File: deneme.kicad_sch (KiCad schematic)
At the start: 60 parts, among them J1 USB_C_Receptacle_USB2.0_16P, J2 Conn_01x04_Pin, J3 LORA_USART2_SOCKETS, J4 RJ45, SW1 SW_SPDT, U1 STM32F103C8T6, U2 AMS1117-3.3, U3 MAX485E, U4 ESDS302DBVR, U5 USBLC6-2SC6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

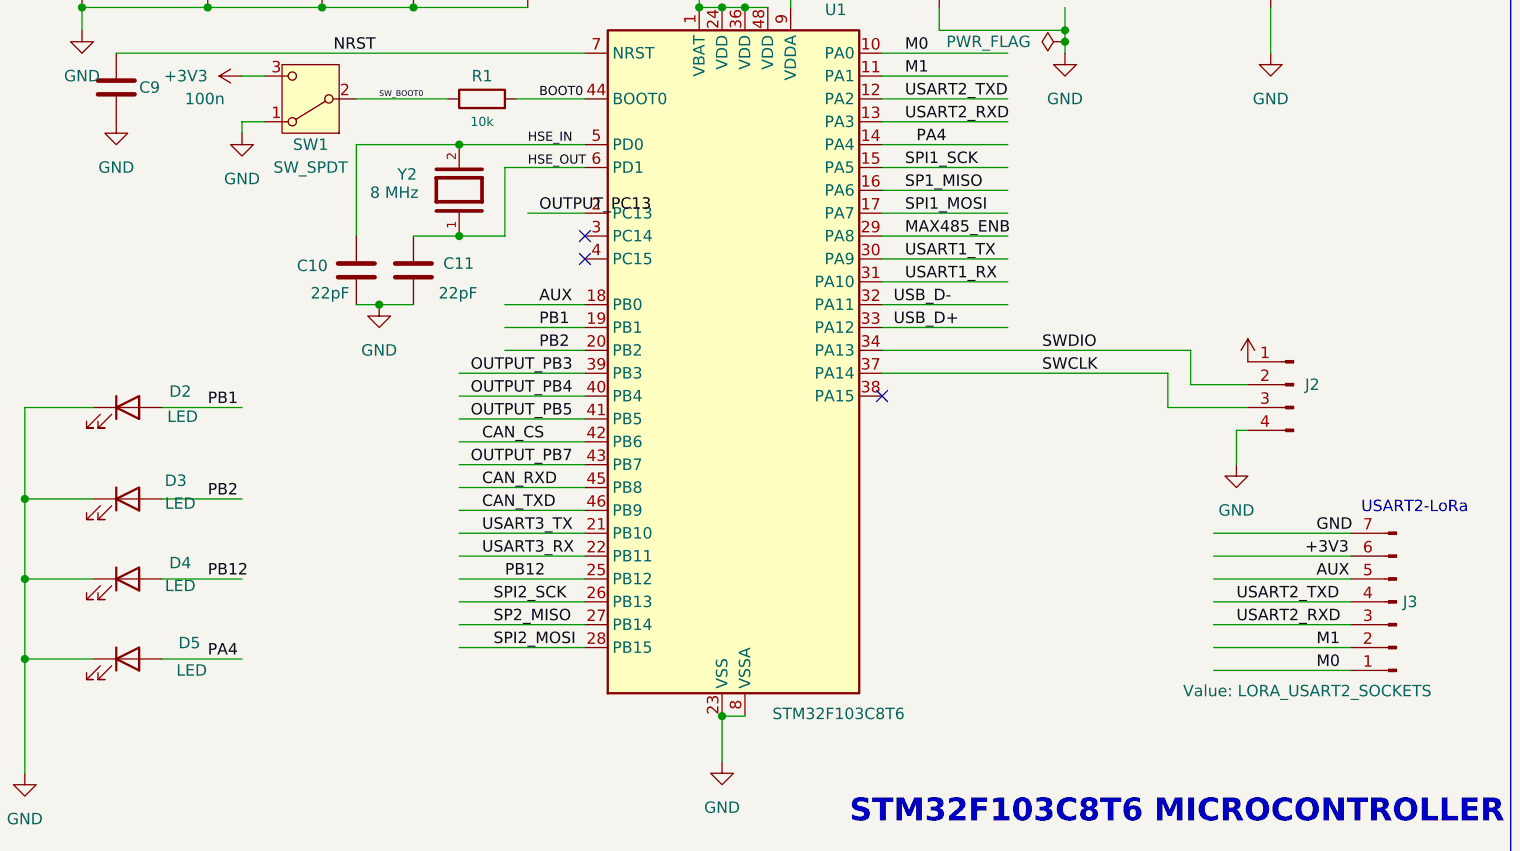
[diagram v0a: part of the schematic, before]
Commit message: added led resistors
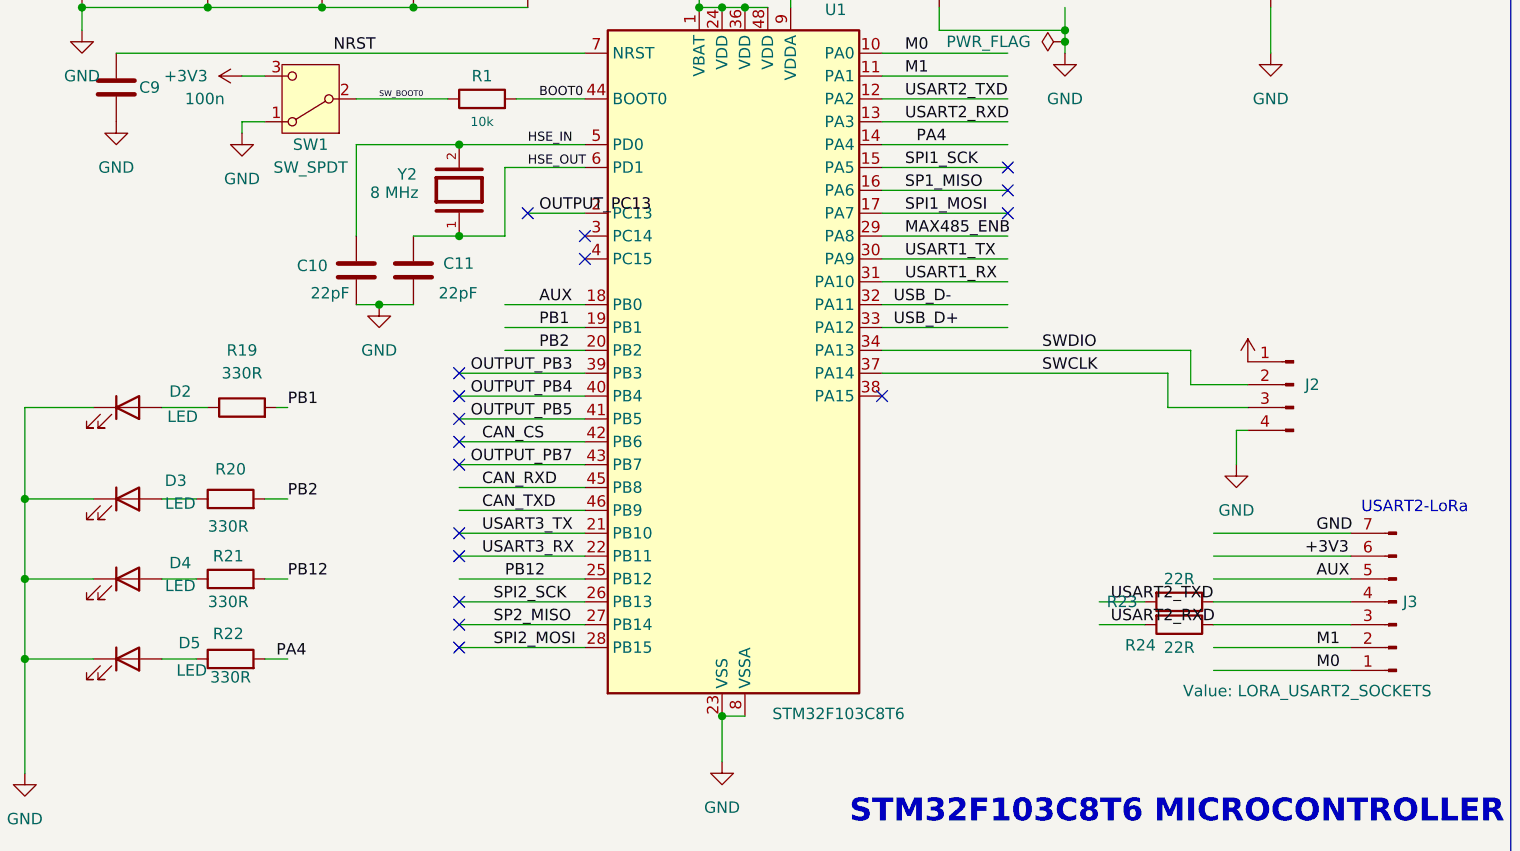
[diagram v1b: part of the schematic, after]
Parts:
- added R19, R20, R21, R22: 330R, Resistor_SMD:R_1206_3216Metric, symbol Device:R
- added R23, R24: 22R, Resistor_SMD:R_1206_3216Metric, symbol Device:R
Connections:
- net PA4: now also R22.2; no longer D5.2 (A)
- net PB1: now also R19.2; no longer D2.2 (A)
- net PB12: now also R21.2; no longer D4.2 (A)
- net PB2: now also R20.2; no longer D3.2 (A)
- net USART2_RXD: now also R24.2; no longer J3.3 (Pin_3)
- net USART2_TXD: now also R23.2; no longer J3.4 (Pin_4)
- new net: D2.2 (A), R19.1
- new net: D4.2 (A), R21.1
- new net: D3.2 (A), R20.1
- new net: J3.3 (Pin_3), R24.1
- new net: D5.2 (A), R22.1
- new net: J3.4 (Pin_4), R23.1
- no-connect marks 12 -> 26
